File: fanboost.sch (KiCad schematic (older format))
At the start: 15 parts, among them SW1 SWITCH_SPDT, U1 LT1308B

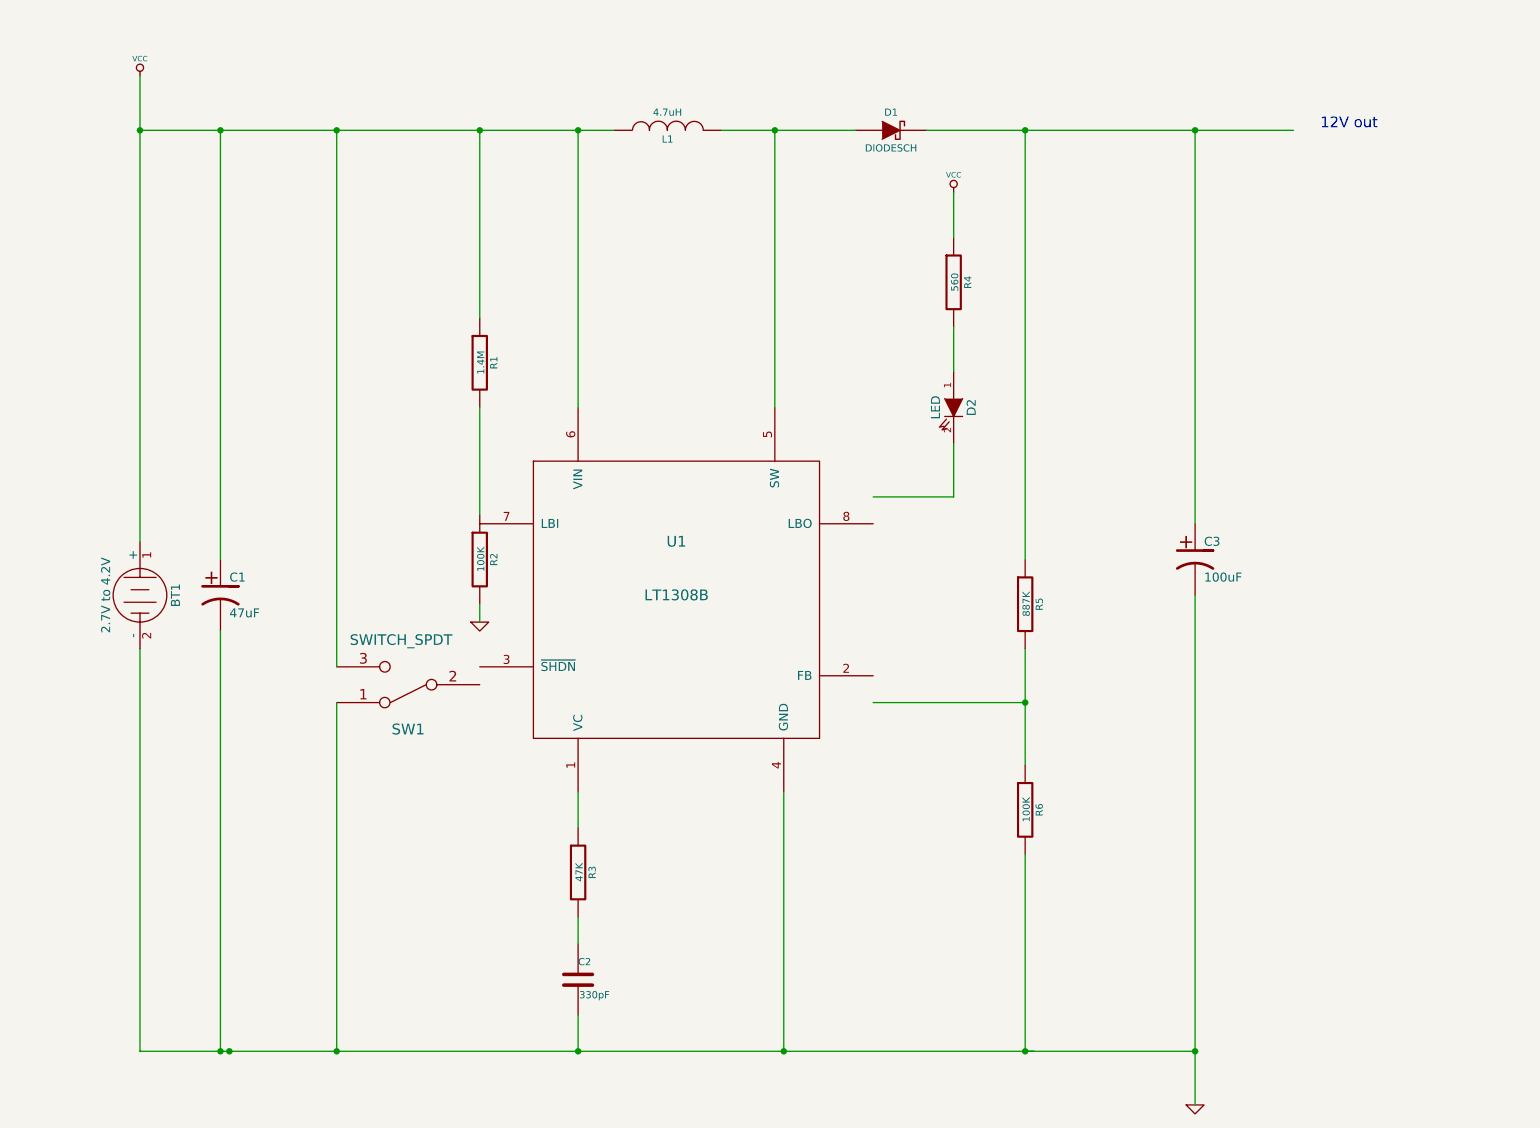
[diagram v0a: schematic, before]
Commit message: Generate netlist, add ltspice simulation
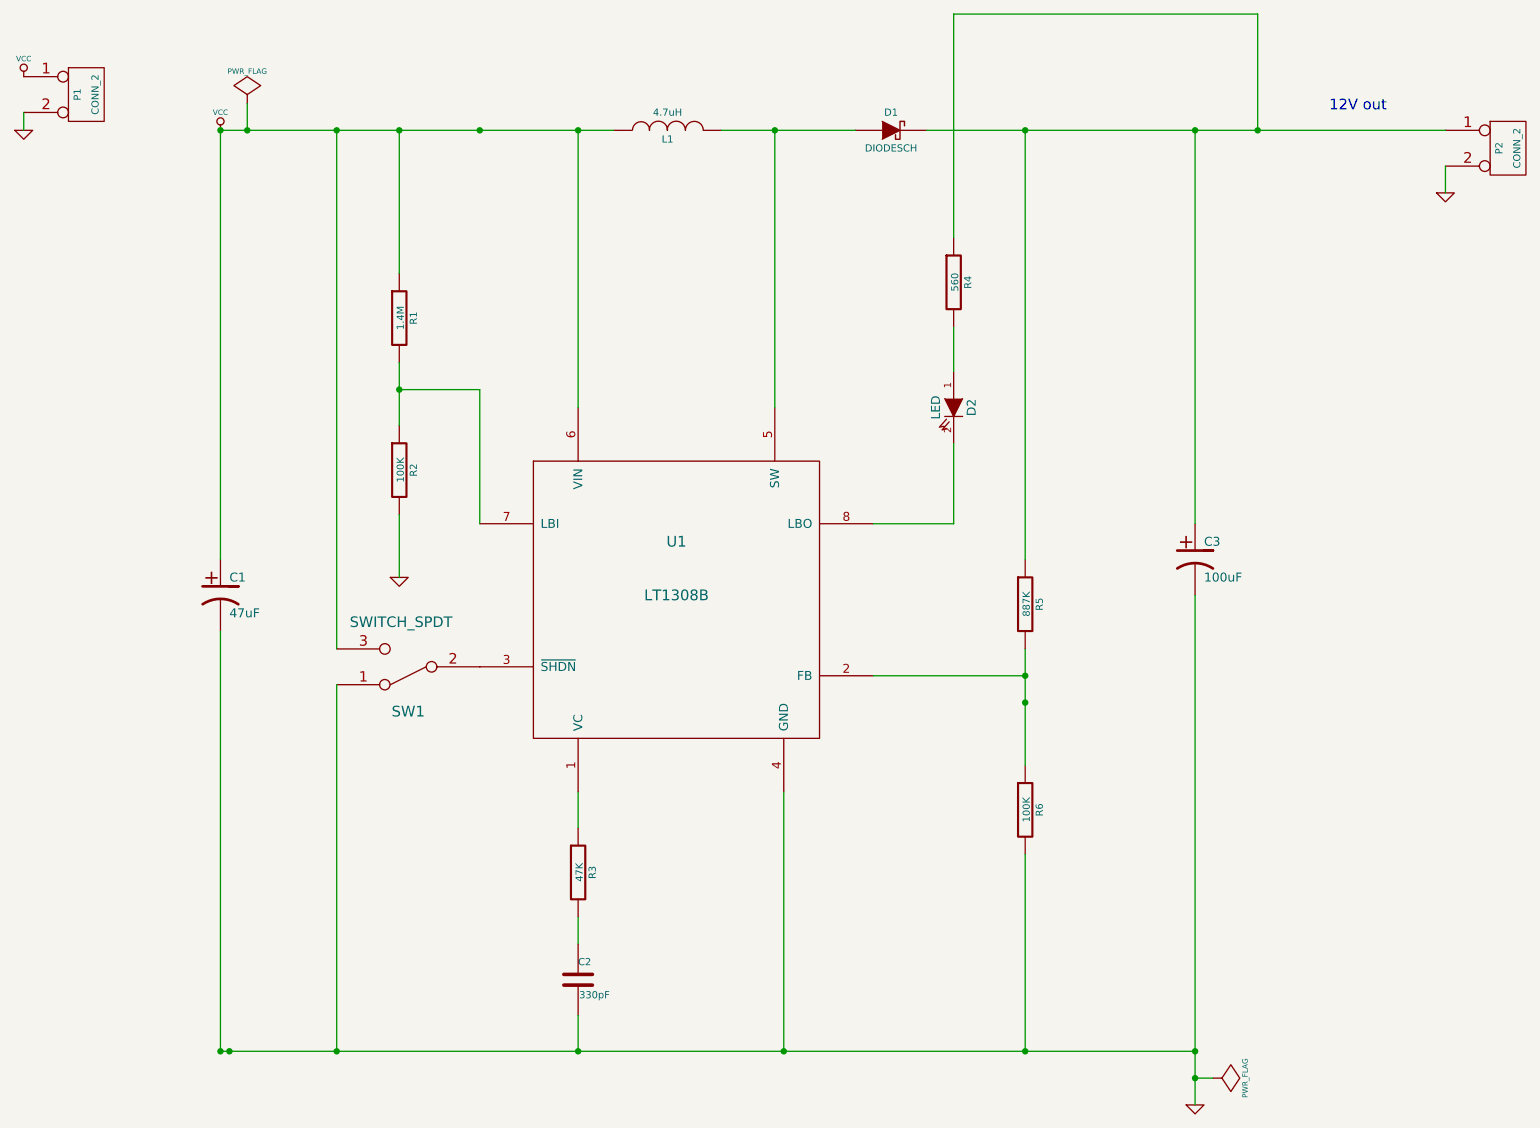
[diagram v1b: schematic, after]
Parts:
- removed BT1: 2.7V to 4.2V, ~, symbol BATTERY
- added P1, P2: CONN_2, symbol CONN_2
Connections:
- wire segments 30 -> 35
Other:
- moved on the sheet: R1, R2, SW1
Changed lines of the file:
@@
 Sheet 1 1
 Title ""
-Date "27 aug 2014"
+Date "29 aug 2014"
 Rev ""
 Comp ""
@@
 Comment4 ""
 $EndDescr
-$Comp
-L BATTERY BT1
-U 1 1 53FD7506
-P 1750 4200
-F 0 "BT1" H 1750 4400 50  0000 C CNN
-F 1 "2.7V to 4.2V" H 1750 4010 50  0000 C CNN
-F 2 "~" H 1750 4200 60  0000 C CNN
-F 3 "~" H 1750 4200 60  0000 C CNN
-	1    1750 4200
-	0    1    1    0
-$EndComp
 $Comp
 L CP1 C1
@@
 $EndComp
 $Comp
-L LT1308B U1
-U 1 1 53FD816B
-P 4750 4200
-F 0 "U1" H 4750 4500 60  0000 C CNN
-F 1 "LT1308B" H 4750 4200 60  0000 C CNN
-F 2 "~" H 4750 4200 60  0000 C CNN
-F 3 "~" H 4750 4200 60  0000 C CNN
-	1    4750 4200
-	1    0    0    -1
-$EndComp
-$Comp
 L R R5
 U 1 1 53FD81A2
@@
 $EndComp
 $Comp
-L GND #PWR4
+L GND #PWR01
 U 1 1 53FD8242
 P 7650 7050
-F 0 "#PWR4" H 7650 7050 30  0001 C CNN
+F 0 "#PWR01" H 7650 7050 30  0001 C CNN
 F 1 "GND" H 7650 6980 30  0001 C CNN
 F 2 "" H 7650 7050 60  0000 C CNN
@@
 L SWITCH_SPDT SW1
 U 1 1 53FD89C8
-P 3250 4700
-F 0 "SW1" H 3250 4950 60  0000 C CNN
-F 1 "SWITCH_SPDT" H 3290 4450 59  0000 C CNN
-F 2 "" H 3250 4700 60  0000 C CNN
-F 3 "" H 3250 4700 60  0000 C CNN
-	1    3250 4700
+P 3250 4600
+F 0 "SW1" H 3250 4850 60  0000 C CNN
+F 1 "SWITCH_SPDT" H 3290 4350 59  0000 C CNN
+F 2 "" H 3250 4600 60  0000 C CNN
+F 3 "" H 3250 4600 60  0000 C CNN
+	1    3250 4600
 	-1   0    0    1
 $EndComp
@@
 L R R1
 U 1 1 53FD8AE9
-P 3650 2900
-F 0 "R1" V 3730 2900 40  0000 C CNN
-F 1 "1.4M" V 3657 2901 40  0000 C CNN
-F 2 "~" V 3580 2900 30  0000 C CNN
-F 3 "~" H 3650 2900 30  0000 C CNN
-	1    3650 2900
-	1    0    0    -1
-$EndComp
-$Comp
-L GND #PWR2
+P 3200 2650
+F 0 "R1" V 3280 2650 40  0000 C CNN
+F 1 "1.4M" V 3207 2651 40  0000 C CNN
+F 2 "~" V 3130 2650 30  0000 C CNN
+F 3 "~" H 3200 2650 30  0000 C CNN
+	1    3200 2650
+	1    0    0    -1
+$EndComp
+$Comp
+L GND #PWR02
 U 1 1 53FD8BA4
-P 3650 4350
-F 0 "#PWR2" H 3650 4350 30  0001 C CNN
-F 1 "GND" H 3650 4280 30  0001 C CNN
-F 2 "" H 3650 4350 60  0000 C CNN
-F 3 "" H 3650 4350 60  0000 C CNN
-	1    3650 4350
+P 3200 4100
+F 0 "#PWR02" H 3200 4100 30  0001 C CNN
+F 1 "GND" H 3200 4030 30  0001 C CNN
+F 2 "" H 3200 4100 60  0000 C CNN
+F 3 "" H 3200 4100 60  0000 C CNN
+	1    3200 4100
 	1    0    0    -1
 $EndComp
@@
 L R R2
 U 1 1 53FD8BB3
-P 3650 4000
-F 0 "R2" V 3730 4000 40  0000 C CNN
-F 1 "100K" V 3657 4001 40  0000 C CNN
-F 2 "~" V 3580 4000 30  0000 C CNN
-F 3 "~" H 3650 4000 30  0000 C CNN
-	1    3650 4000
-	1    0    0    -1
-$EndComp
-$Comp
-L VCC #PWR1
-U 1 1 53FD8D41
-P 1750 1300
-F 0 "#PWR1" H 1750 1400 30  0001 C CNN
-F 1 "VCC" H 1750 1400 30  0000 C CNN
-F 2 "" H 1750 1300 60  0000 C CNN
-F 3 "" H 1750 1300 60  0000 C CNN
-	1    1750 1300
-	1    0    0    -1
-$EndComp
-$Comp
-L VCC #PWR3
-U 1 1 53FD8D7B
-P 6300 1950
-F 0 "#PWR3" H 6300 2050 30  0001 C CNN
-F 1 "VCC" H 6300 2050 30  0000 C CNN
-F 2 "" H 6300 1950 60  0000 C CNN
-F 3 "" H 6300 1950 60  0000 C CNN
-	1    6300 1950
+P 3200 3500
+F 0 "R2" V 3280 3500 40  0000 C CNN
+F 1 "100K" V 3207 3501 40  0000 C CNN
+F 2 "~" V 3130 3500 30  0000 C CNN
+F 3 "~" H 3200 3500 30  0000 C CNN
+	1    3200 3500
 	1    0    0    -1
 $EndComp
@@
 	0    1    1    0
 $EndComp
+Text Notes 8400 1500 0    60   ~ 0
+12V out\n
+$Comp
+L CONN_2 P1
+U 1 1 54000A69
+P 1450 1400
+F 0 "P1" V 1400 1400 40  0000 C CNN
+F 1 "CONN_2" V 1500 1400 40  0000 C CNN
+F 2 "" H 1450 1400 60  0000 C CNN
+F 3 "" H 1450 1400 60  0000 C CNN
+	1    1450 1400
+	1    0    0    -1
+$EndComp
+$Comp
+L GND #PWR03
+U 1 1 54000AB6
+P 1100 1600
+F 0 "#PWR03" H 1100 1600 30  0001 C CNN
+F 1 "GND" H 1100 1530 30  0001 C CNN
+F 2 "" H 1100 1600 60  0000 C CNN
+F 3 "" H 1100 1600 60  0000 C CNN
+	1    1100 1600
+	1    0    0    -1
+$EndComp
 Wire Wire Line
 	5000 1600 5750 1600
-Wire Wire Line
-	5850 4800 6700 4800
 Wire Wire Line
 	6700 4500 6700 5150
 Connection ~ 6700 4800
 Wire Wire Line
-	6150 1600 8200 1600
-Wire Wire Line
-	1750 4500 1750 6750
-Wire Wire Line
-	1750 6750 6750 6750
-Wire Wire Line
-	6700 6750 7650 6750
-Wire Wire Line
-	7650 4200 7650 7050
+	2200 6750 7650 6750
 Connection ~ 7650 6750
 Wire Wire Line
@@
 	5350 5300 5350 6750
 Connection ~ 5350 6750
-Wire Wire Line
-	4200 5300 4200 5500
 Connection ~ 2250 6750
 Wire Wire Line
@@
 	2200 4400 2200 6750
 Connection ~ 2200 6750
-Wire Wire Line
-	2850 4800 2850 6750
 Connection ~ 2850 6750
 Wire Wire Line
-	3650 3150 3650 3750
-Wire Wire Line
-	3650 4250 3650 4350
-Connection ~ 1750 1600
-Wire Wire Line
-	1750 1300 1750 3900
-Wire Wire Line
 	2200 1600 2200 4000
-Wire Wire Line
-	1750 1600 4400 1600
-Wire Wire Line
-	2850 1600 2850 4600
 Connection ~ 2850 1600
-Wire Wire Line
-	3650 1600 3650 2650
 Connection ~ 3650 1600
 Wire Wire Line
@@
 Connection ~ 6700 1600
 Wire Wire Line
-	6300 1950 6300 2200
-Wire Wire Line
 	6300 2700 6300 2950
-Wire Wire Line
-	6300 3350 6300 3650
-Wire Wire Line
-	6300 3650 5850 3650
 Wire Wire Line
 	7650 3800 7650 1600
 Connection ~ 7650 1600
-Text Notes 8350 1600 0    60   ~ 0
-12V out\n
+Wire Wire Line
+	7650 7050 7650 4200
+Wire Wire Line
+	4200 5300 4200 5500
+Wire Wire Line
+	1100 1500 1100 1600
+Wire Wire Line
+	2200 1600 4400 1600
+Wire Wire Line
+	8000 1600 8000 950
+Wire Wire Line
+	8000 950  6300 950
+Wire Wire Line
+	6300 950  6300 2200
+Connection ~ 8000 1600
+$Comp
+L LT1308B U1
+U 1 1 5400115E
+P 4750 4200
+F 0 "U1" H 4750 4500 60  0000 C CNN
+F 1 "LT1308B" H 4750 4200 60  0000 C CNN
+F 2 "~" H 4750 4200 60  0000 C CNN
+F 3 "~" H 4750 4200 60  0000 C CNN
+	1    4750 4200
+	1    0    0    -1
+$EndComp
+Wire Wire Line
+	2850 4500 2850 1600
+Wire Wire Line
+	2850 4700 2850 6750
+Wire Wire Line
+	5850 4650 6700 4650
+Connection ~ 6700 4650
+Wire Wire Line
+	5850 3800 6300 3800
+Wire Wire Line
+	6300 3800 6300 3350
+Wire Wire Line
+	3200 1600 3200 2400
+Connection ~ 3200 1600
+Wire Wire Line
+	3200 2900 3200 3250
+Wire Wire Line
+	3200 3750 3200 4100
+Wire Wire Line
+	3650 3800 3650 3050
+Wire Wire Line
+	3650 3050 3200 3050
+Connection ~ 3200 3050
+$Comp
+L PWR_FLAG #FLG04
+U 1 1 540013A2
+P 7750 6900
+F 0 "#FLG04" H 7750 6995 30  0001 C CNN
+F 1 "PWR_FLAG" H 7750 7080 30  0000 C CNN
+F 2 "" H 7750 6900 60  0000 C CNN
+F 3 "" H 7750 6900 60  0000 C CNN
+	1    7750 6900
+	0    1    1    0
+$EndComp
+Wire Wire Line
+	7650 6900 7750 6900
+Connection ~ 7650 6900
+$Comp
+L VCC #PWR05
+U 1 1 54001A23
+P 1100 1300
+F 0 "#PWR05" H 1100 1400 30  0001 C CNN
+F 1 "VCC" H 1100 1400 30  0000 C CNN
+F 2 "" H 1100 1300 60  0000 C CNN
+F 3 "" H 1100 1300 60  0000 C CNN
+	1    1100 1300
+	1    0    0    -1
+$EndComp
+$Comp
+L VCC #PWR06
+U 1 1 54001A32
+P 2200 1600
+F 0 "#PWR06" H 2200 1700 30  0001 C CNN
+F 1 "VCC" H 2200 1700 30  0000 C CNN
+F 2 "" H 2200 1600 60  0000 C CNN
+F 3 "" H 2200 1600 60  0000 C CNN
+	1    2200 1600
+	1    0    0    -1
+$EndComp
+$Comp
+L PWR_FLAG #FLG07
+U 1 1 54001A4F
+P 2350 1450
+F 0 "#FLG07" H 2350 1545 30  0001 C CNN
+F 1 "PWR_FLAG" H 2350 1630 30  0000 C CNN
+F 2 "" H 2350 1450 60  0000 C CNN
+F 3 "" H 2350 1450 60  0000 C CNN
+	1    2350 1450
+	1    0    0    -1
+$EndComp
+Wire Wire Line
+	2350 1450 2350 1600
+Connection ~ 2350 1600
+$Comp
+L CONN_2 P2
+U 1 1 54001C67
+P 9400 1700
+F 0 "P2" V 9350 1700 40  0000 C CNN
+F 1 "CONN_2" V 9450 1700 40  0000 C CNN
+F 2 "" H 9400 1700 60  0000 C CNN
+F 3 "" H 9400 1700 60  0000 C CNN
+	1    9400 1700
+	1    0    0    -1
+$EndComp
+$Comp
+L GND #PWR08
+U 1 1 54001CB0
+P 9050 1950
+F 0 "#PWR08" H 9050 1950 30  0001 C CNN
+F 1 "GND" H 9050 1880 30  0001 C CNN
+F 2 "" H 9050 1950 60  0000 C CNN
+F 3 "" H 9050 1950 60  0000 C CNN
+	1    9050 1950
+	1    0    0    -1
+$EndComp
+Wire Wire Line
+	6150 1600 9050 1600
+Wire Wire Line
+	9050 1800 9050 1950
 $EndSCHEMATC

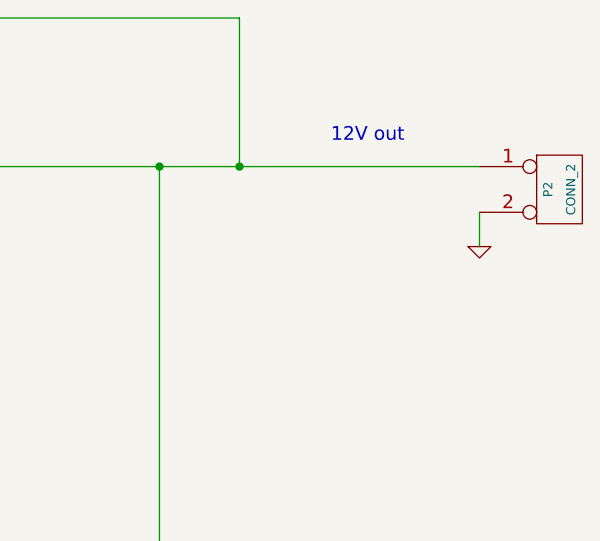
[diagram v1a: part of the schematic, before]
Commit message: Add some footprints
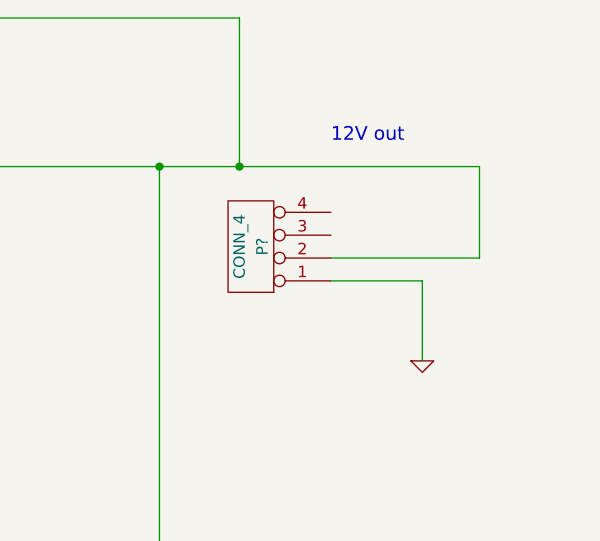
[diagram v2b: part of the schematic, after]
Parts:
- removed P2: CONN_2, symbol CONN_2
- added P?: CONN_4, symbol CONN_4
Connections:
- net GND: now also P?.1 (P1)
- net at C3.1, D1.2 (K), R4.1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: now also P?.2 (P2)
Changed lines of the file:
@@
 LIBS:fanboost
 LIBS:switch_spdt
+LIBS:vishay
+LIBS:vishay-1
 LIBS:fanboost-cache
 EELAYER 27 0
@@
 Sheet 1 1
 Title ""
-Date "29 aug 2014"
+Date "21 sep 2014"
 Rev ""
 Comp ""
@@
 Connection ~ 2350 1600
 $Comp
-L CONN_2 P2
-U 1 1 54001C67
-P 9400 1700
-F 0 "P2" V 9350 1700 40  0000 C CNN
-F 1 "CONN_2" V 9450 1700 40  0000 C CNN
-F 2 "" H 9400 1700 60  0000 C CNN
-F 3 "" H 9400 1700 60  0000 C CNN
-	1    9400 1700
-	1    0    0    -1
-$EndComp
-$Comp
 L GND #PWR08
 U 1 1 54001CB0
-P 9050 1950
-F 0 "#PWR08" H 9050 1950 30  0001 C CNN
-F 1 "GND" H 9050 1880 30  0001 C CNN
-F 2 "" H 9050 1950 60  0000 C CNN
-F 3 "" H 9050 1950 60  0000 C CNN
-	1    9050 1950
+P 8800 2450
+F 0 "#PWR08" H 8800 2450 30  0001 C CNN
+F 1 "GND" H 8800 2380 30  0001 C CNN
+F 2 "" H 8800 2450 60  0000 C CNN
+F 3 "" H 8800 2450 60  0000 C CNN
+	1    8800 2450
 	1    0    0    -1
 $EndComp
 Wire Wire Line
 	6150 1600 9050 1600
-Wire Wire Line
-	9050 1800 9050 1950
+$Comp
+L CONN_4 P?
+U 1 1 541E1C40
+P 8050 1950
+F 0 "P?" V 8000 1950 50  0000 C CNN
+F 1 "CONN_4" V 8100 1950 50  0000 C CNN
+F 2 "" H 8050 1950 60  0000 C CNN
+F 3 "" H 8050 1950 60  0000 C CNN
+	1    8050 1950
+	-1   0    0    1
+$EndComp
+Wire Wire Line
+	8400 2100 8800 2100
+Wire Wire Line
+	8800 2100 8800 2450
+Wire Wire Line
+	9050 1600 9050 2000
+Wire Wire Line
+	9050 2000 8400 2000
 $EndSCHEMATC
